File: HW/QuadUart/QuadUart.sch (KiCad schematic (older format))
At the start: 93 parts, among them J1 USB_C_Receptacle_USB2.0, J2 Conn_02x05_Odd_Even, J3 Conn_02x10_Odd_Even, Q1 BC847, Q2 BC847, SW1 SW_DIP_x04, SW2 SW_DIP_x01, SW3 SW_DIP_x01, U1 LN1134-3.3V, U10 SN74LV4T125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

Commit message: Finished layout, added Gerbers
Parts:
- removed C7, C8: 27pF, Capacitor_SMD:C_0603_1608Metric_Pad1.08x0.95mm_HandSolder, symbol Device:C
- removed Y1: Crystal_GND24, Crystal:Crystal_SMD_3225-4Pin_3.2x2.5mm, symbol Device:Crystal_GND24
- added D11: LED, LED_SMD:LED_0603_1608Metric_Pad1.05x0.95mm_HandSolder, symbol Device:LED
- added J4: Conn_01x05, Connector_PinHeader_2.54mm:PinHeader_1x05_P2.54mm_Vertical, symbol Connector_Generic:Conn_01x05
- added LOGO1: Logo_Open_Hardware_Small, Symbol:OSHW-Logo_7.5x8mm_SilkScreen, symbol Graphic:Logo_Open_Hardware_Small
- added MARK1: LOGO, Kicad_Library:FOX_LOGO_MASK, symbol Kicad_Library:LOGO
- added MARK2: LOGO, Kicad_Library:FOX_LOGO_SILK, symbol Kicad_Library:LOGO
- added R31: 0R, Resistor_SMD:R_0603_1608Metric_Pad0.98x0.95mm_HandSolder, symbol Device:R
- added R32: R, Resistor_SMD:R_0603_1608Metric_Pad0.98x0.95mm_HandSolder, symbol Device:R
- added Y1: Crystal_GND2, Crystal:Resonator_SMD_muRata_CSTxExxV-3Pin_3.0x1.1mm, symbol Device:Crystal_GND2
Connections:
- net +3V3: now also C15.1, U10.14 (VCC), J4.2 (Pin_2), R32.2; no longer C17.1, U9.14 (VCC)
- net D+: now also U4.1 (IO1); no longer U4.4 (IO3), U4.6 (IO4)
- net D-: now also U4.6 (IO4); no longer U4.1 (IO1), U4.3 (IO2)
- net DTR_1_RES: now also U9.12; no longer U10.8
- net DTR_1_UC: now also U9.11; no longer U10.9
- net DTR_2_RES: now also U9.8; no longer U10.12
- net DTR_2_UC: now also U9.9; no longer U10.11
- net DTR_3_UC: now also U7.11 (AN5/C1IN+/VBUSON/CN7/RB5); no longer U7.54 (CN15/RD6)
- net DTR_4_UC: now also U7.12 (AN4/C1IN-/CN6/RB4); no longer U7.55 (CN16/RD7)
- net GND: now also D11.1 (K), J4.3 (Pin_3), Y1.2
- net LED_RX_1: now also U7.2 (PMD6/RE6); no longer U7.61 (PMD1/RE1)
- net LED_RX_2: now also U7.64 (PMD4/RE4); no longer U7.63 (PMD3/RE3)
- net LED_RX_3: now also U7.14 (AN2/C2IN-/CN4/RB2); no longer U7.1 (PMD5/RE5)
- net LED_RX_4: now also U7.16 (PGED1/AN0/VREF+/CVREF+/PMA6/CN2/RB0); no longer U7.3 (PMD7/RE7)
- net LED_TX_1: now also U7.3 (PMD7/RE7); no longer U7.60 (PMD0/RE0)
- net LED_TX_2: now also U7.1 (PMD5/RE5); no longer U7.62 (PMD2/RE2)
- net LED_TX_3: now also U7.13 (AN3/C2IN+/CN5/RB3); no longer U7.64 (PMD4/RE4)
- net LED_TX_4: now also U7.15 (PGEC1/AN1/VREF-/CVREF-/CN3/RB1); no longer U7.2 (PMD6/RE6)
- net OSC1: now also Y1.1
- net OSC2: now also R31.2
- net PWR_1: now also R14.2
- net PWR_2: now also R16.2
- net RX_1_RES: now also U10.5, U2.3 (IO2); no longer U2.6 (IO4), U9.2
- net RX_1_UC: now also U10.6, U7.5 (SDA4/SDI2/U3RX/PMA4/CN9/RG7); no longer U7.50 (SDA3/SDI3/U1RX/OC3/RD2), U9.3
- net RX_2_RES: now also U10.2, U2.1 (IO1); no longer U2.4 (IO3), U9.5
- net RX_2_UC: now also U10.3, U7.8 (~SS2~/U6RX/~U3CTS~/PMA2/CN11/RG9); no longer U7.31 (AC1TX/SDA5/SDI4/U2RX/PMA9/CN17/RF4), U9.6
- net RX_3_RES: now also U10.11, U6.6 (IO4); no longer U3.6 (IO4), U9.9
- net RX_3_UC: now also U10.12, U7.31 (AC1TX/SDA5/SDI4/U2RX/PMA9/CN17/RF4); no longer U7.5 (SDA4/SDI2/U3RX/PMA4/CN9/RG7), U9.8
- net RX_4_RES: now also U10.9, U6.4 (IO3); no longer U3.4 (IO3), U9.11
- net RX_4_UC: now also U10.8, U7.21 (AN8/~SS4~/U5RX/~U2CTS~/C1OUT/RB8); no longer U7.43 (~SS3~/U4RX/~U1CTS~/SDA1/IC2/INT2/RD9), U9.12
- net RX_DBG: now also U7.50 (SDA3/SDI3/U1RX/OC3/RD2); no longer U7.8 (~SS2~/U6RX/~U3CTS~/PMA2/CN11/RG9)
- net TX_1_RES: now also U2.6 (IO4), U9.6; no longer U10.3, U2.3 (IO2)
- net TX_1_UC: now also U7.6 (SCL4/SDO2/U3TX/PMA3/CN10/RG8), U9.5; no longer U10.2, U7.51 (SCL3/SDO3/U1TX/OC4/RD3)
- net TX_2_RES: now also U2.4 (IO3), U9.3; no longer U10.6, U2.1 (IO1)
- net TX_2_UC: now also U7.4 (SCK2/U6TX/~U3RTS~/PMA5/CN8/RG6), U9.2; no longer U10.5, U7.32 (AC1RX/SCL5/SDO4/U2TX/PMA8/CN18/RF5)
- net TX_3_RES: now also U11.6, U3.6 (IO4); no longer U11.3, U3.3 (IO2)
- net TX_3_UC: now also U11.5, U7.32 (AC1RX/SCL5/SDO4/U2TX/PMA8/CN18/RF5); no longer U11.2, U7.6 (SCL4/SDO2/U3TX/PMA3/CN10/RG8)
- net TX_4_RES: now also U11.3, U3.4 (IO3); no longer U11.6, U3.1 (IO1)
- net TX_4_UC: now also U11.2, U7.29 (AN14/SCK4/U5TX/~U2RTS~/PMALH/PMA1/RB14); no longer U11.5, U7.49 (SCK3/U4TX/~U1RTS~/OC2/RD1)
- net TX_DBG: now also U7.51 (SCL3/SDO3/U1TX/OC4/RD3); no longer U7.4 (SCK2/U6TX/~U3RTS~/PMA5/CN8/RG6)
- net VCC: now also C17.1, SW3.1, U9.14 (VCC); no longer C15.1, R14.2, SW3.2, U10.14 (VCC)
- net VDD: now also SW2.1; no longer R16.2, SW2.2
- net ~MCLR~: now also J4.1 (Pin_1)
- net at C11.1, C12.1, C13.1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: now also SW2.2, SW3.2; no longer SW2.1, SW3.1
- net PGEC2: now reaches U7.17 (PGEC2/AN6/OCFA/RB6)
- net PGEC2: now also J4.5 (Pin_5)
- net PGED2: now reaches U7.18 (PGED2/AN7/RB7)
- net PGED2: now also J4.4 (Pin_4)
- new net: R31.1, Y1.3
- new net: D11.2 (A), R32.1
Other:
- note added: "ICSP "just-in-case" connector"
- note added: "JTAG Programming connector"
- note removed: "Programming connector"
- moved on the sheet: C15, C17, C6, H1, H2, H3, H4, R3, R4, U10A, U10B, U10C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

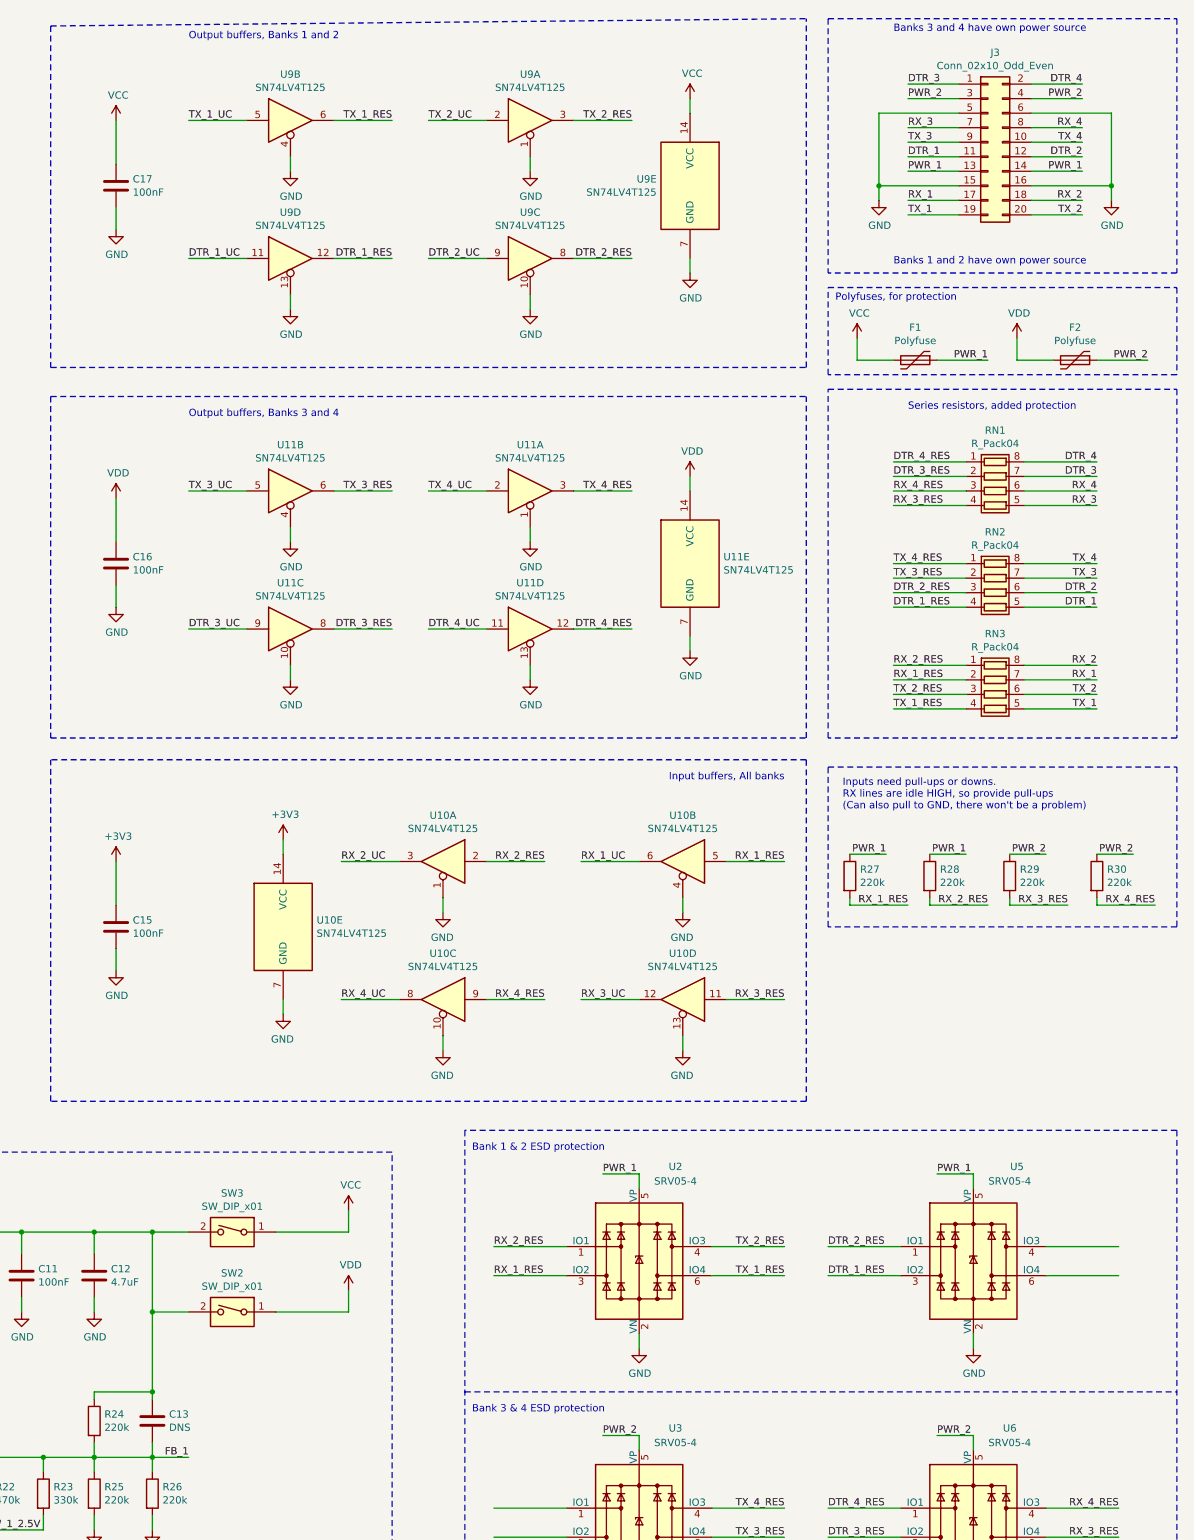
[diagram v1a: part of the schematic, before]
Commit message: Added 2 capacitors (ESD) and changed fuse position.
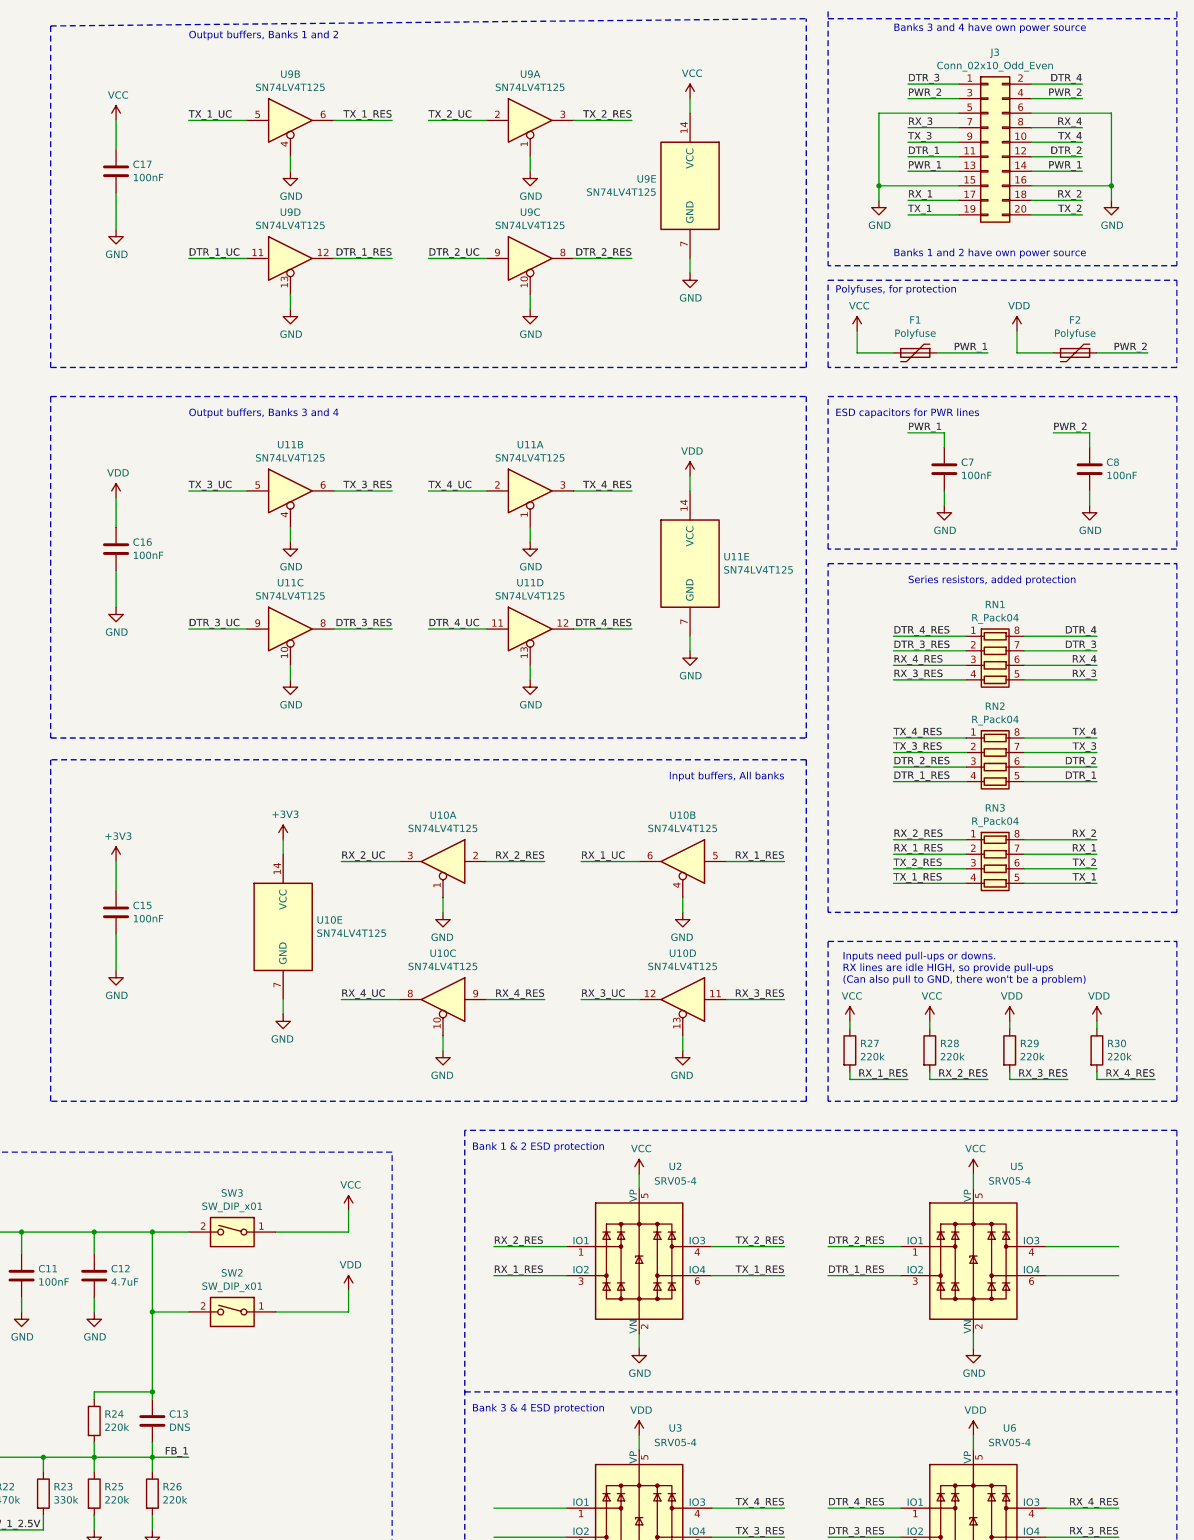
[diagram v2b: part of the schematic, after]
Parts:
- added C7, C8: 100nF, Capacitor_SMD:C_0603_1608Metric_Pad1.08x0.95mm_HandSolder, symbol Device:C
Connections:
- net GND: now also C7.2, C8.2
- net PWR_1: now also C7.1; no longer R27.1, R28.1, U2.5 (VP), U5.5 (VP)
- net PWR_2: now also C8.1; no longer R29.1, R30.1, U3.5 (VP), U6.5 (VP)
- net VCC: now also R27.1, R28.1, U2.5 (VP), U5.5 (VP)
- net VDD: now also R29.1, R30.1, U3.5 (VP), U6.5 (VP)
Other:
- note added: "ESD capacitors for PWR lines"
- moved on the sheet: C15, C16, C17, F1, F2, R27, R28, R29, R30, RN1, RN2, RN3
